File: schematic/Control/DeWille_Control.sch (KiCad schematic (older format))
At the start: 24 parts, among them J101 HN2x10, J102 HN2x10, J103 HN2x10, U101 Logo

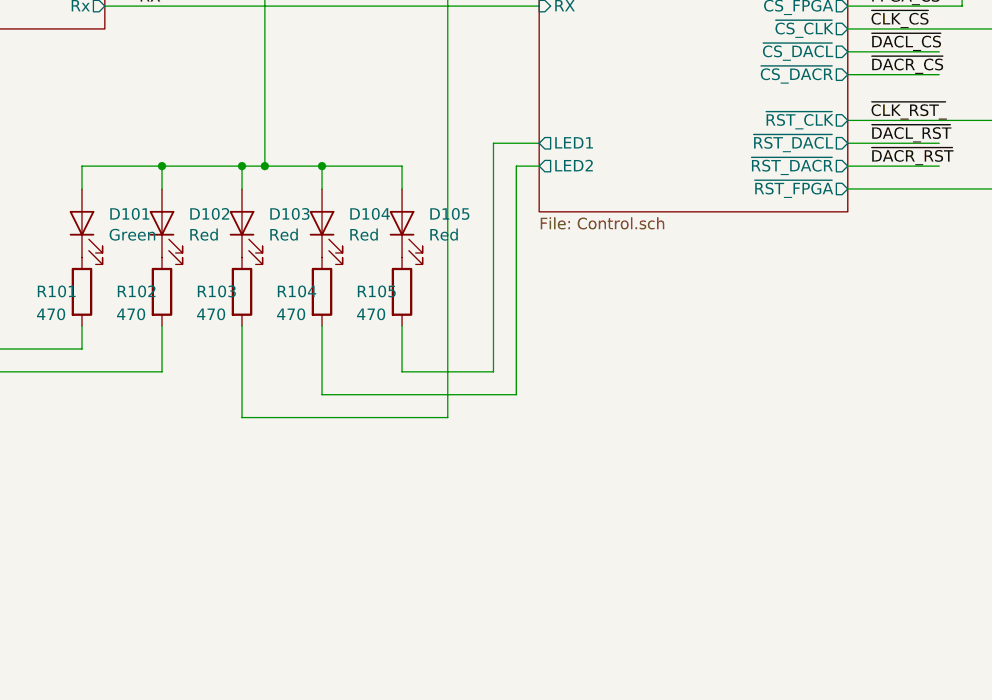
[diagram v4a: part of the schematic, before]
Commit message: Add some testpads. Fix +3V3_FPGA track mix-up after termination addition.
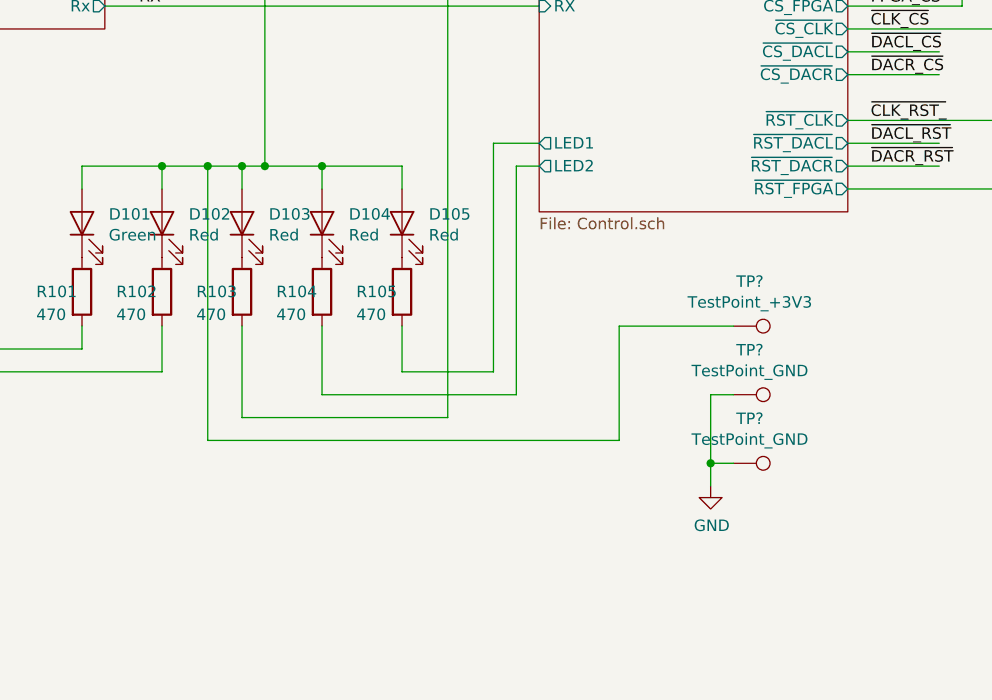
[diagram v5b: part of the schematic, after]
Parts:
- added TP? (x2): TestPoint_GND, TestPoint:TestPoint_THTPad_D2.0mm_Drill1.0mm, symbol Connector:TestPoint
- added TP?: TestPoint_+3V3, TestPoint:TestPoint_THTPad_D2.0mm_Drill1.0mm, symbol Connector:TestPoint
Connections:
- wire segments 227 -> 236
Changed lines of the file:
@@
 Connection ~ 5050 7300
 Wire Wire Line
-	4350 7300 4700 7300
+	4350 7300 4550 7300
 Wire Wire Line
 	4000 8100 2550 8100
@@
 	1    0    0    -1
 $EndComp
+$Comp
+L Connector:TestPoint TP?
+U 1 1 5DE66F70
+P 6850 8600
+AR Path="/5DCFEDFC/5DE66F70" Ref="TP?"  Part="1"
+AR Path="/5DE66F70" Ref="TP?"  Part="1"
+F 0 "TP?" V 7045 8672 50  0000 C CNN
+F 1 "TestPoint_GND" V 6954 8672 50  0000 C CNN
+F 2 "TestPoint:TestPoint_THTPad_D2.0mm_Drill1.0mm" H 7050 8600 50  0001 C CNN
+F 3 "~" H 7050 8600 50  0001 C CNN
+	1    6850 8600
+	0    1    -1   0
+$EndComp
+$Comp
+L Connector:TestPoint TP?
+U 1 1 5DE78F7B
+P 6850 8000
+AR Path="/5DCFEDFC/5DE78F7B" Ref="TP?"  Part="1"
+AR Path="/5DE78F7B" Ref="TP?"  Part="1"
+F 0 "TP?" V 7045 8072 50  0000 C CNN
+F 1 "TestPoint_+3V3" V 6954 8072 50  0000 C CNN
+F 2 "TestPoint:TestPoint_THTPad_D2.0mm_Drill1.0mm" H 7050 8000 50  0001 C CNN
+F 3 "~" H 7050 8000 50  0001 C CNN
+	1    6850 8000
+	0    1    -1   0
+$EndComp
+$Comp
+L Connector:TestPoint TP?
+U 1 1 5DE8BB1B
+P 6850 8300
+AR Path="/5DCFEDFC/5DE8BB1B" Ref="TP?"  Part="1"
+AR Path="/5DE8BB1B" Ref="TP?"  Part="1"
+F 0 "TP?" V 7045 8372 50  0000 C CNN
+F 1 "TestPoint_GND" V 6954 8372 50  0000 C CNN
+F 2 "TestPoint:TestPoint_THTPad_D2.0mm_Drill1.0mm" H 7050 8300 50  0001 C CNN
+F 3 "~" H 7050 8300 50  0001 C CNN
+	1    6850 8300
+	0    1    -1   0
+$EndComp
+$Comp
+L power:GND #PWR?
+U 1 1 5DEB2F33
+P 6750 8700
+AR Path="/5DD2C0D9/5DEB2F33" Ref="#PWR?"  Part="1"
+AR Path="/5DEB2F33" Ref="#PWR?"  Part="1"
+F 0 "#PWR?" H 6750 8450 50  0001 C CNN
+F 1 "GND" H 6755 8527 50  0000 C CNN
+F 2 "" H 6750 8700 50  0001 C CNN
+F 3 "" H 6750 8700 50  0001 C CNN
+	1    6750 8700
+	1    0    0    -1
+$EndComp
+Wire Wire Line
+	6750 8700 6750 8600
+Wire Wire Line
+	6750 8300 6850 8300
+Wire Wire Line
+	6850 8600 6750 8600
+Connection ~ 6750 8600
+Wire Wire Line
+	6750 8600 6750 8300
+Wire Wire Line
+	4550 7300 4550 8500
+Wire Wire Line
+	4550 8500 6350 8500
+Wire Wire Line
+	6350 8500 6350 8000
+Wire Wire Line
+	6350 8000 6850 8000
+Connection ~ 4550 7300
+Wire Wire Line
+	4550 7300 4700 7300
 $EndSCHEMATC

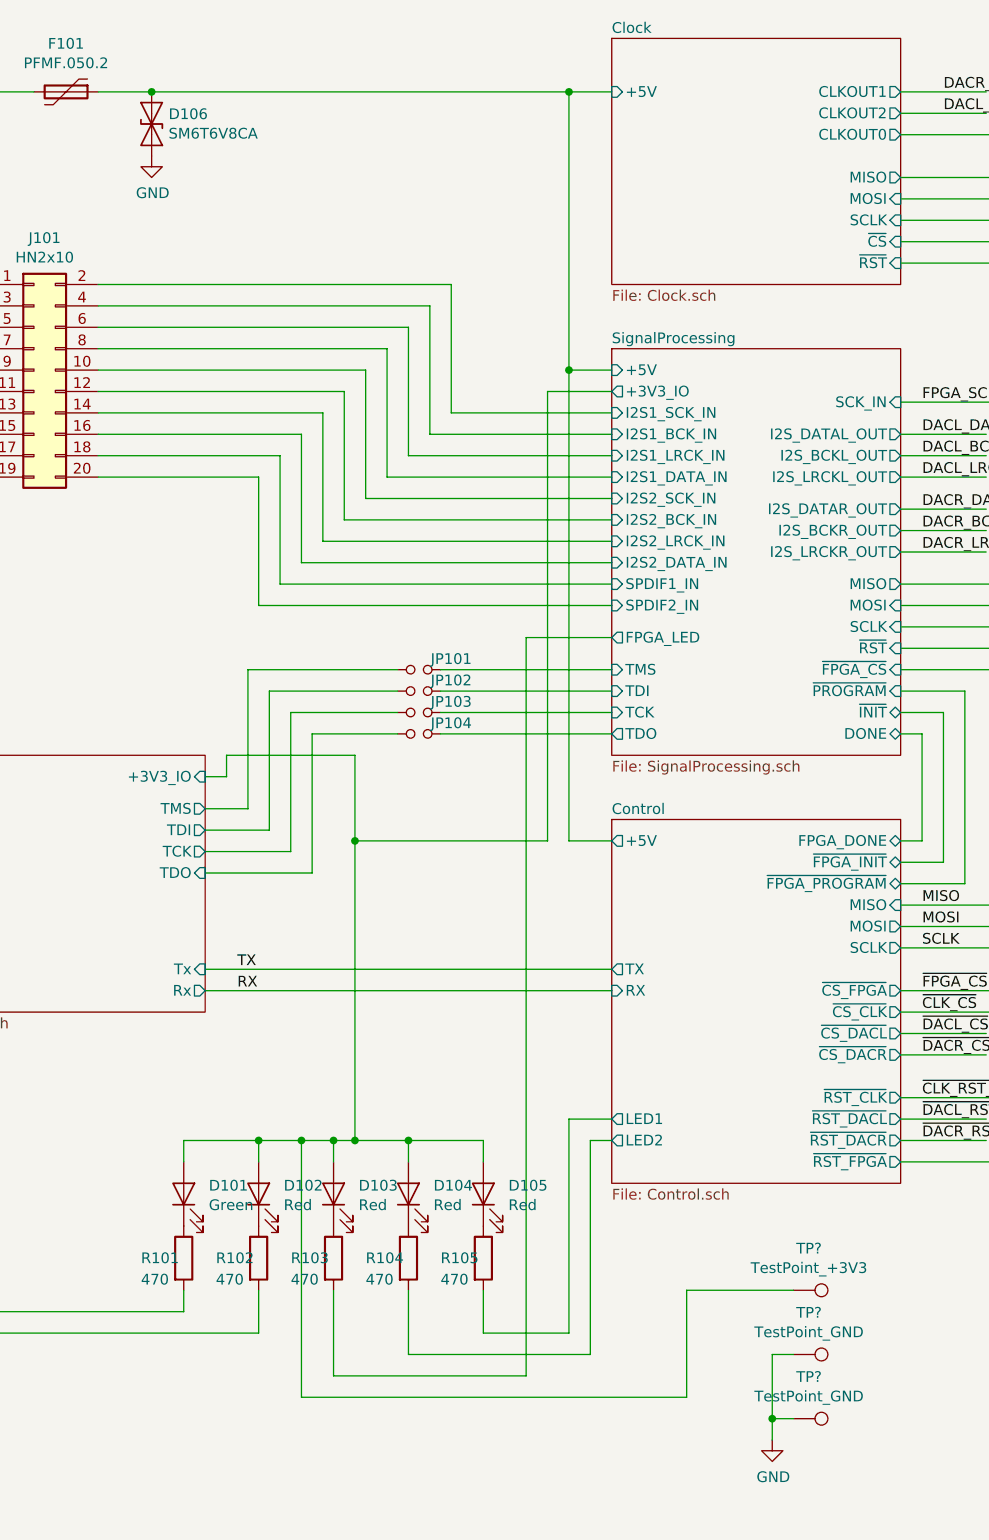
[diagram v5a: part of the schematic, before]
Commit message: Add decoupling cap between +5V and GND
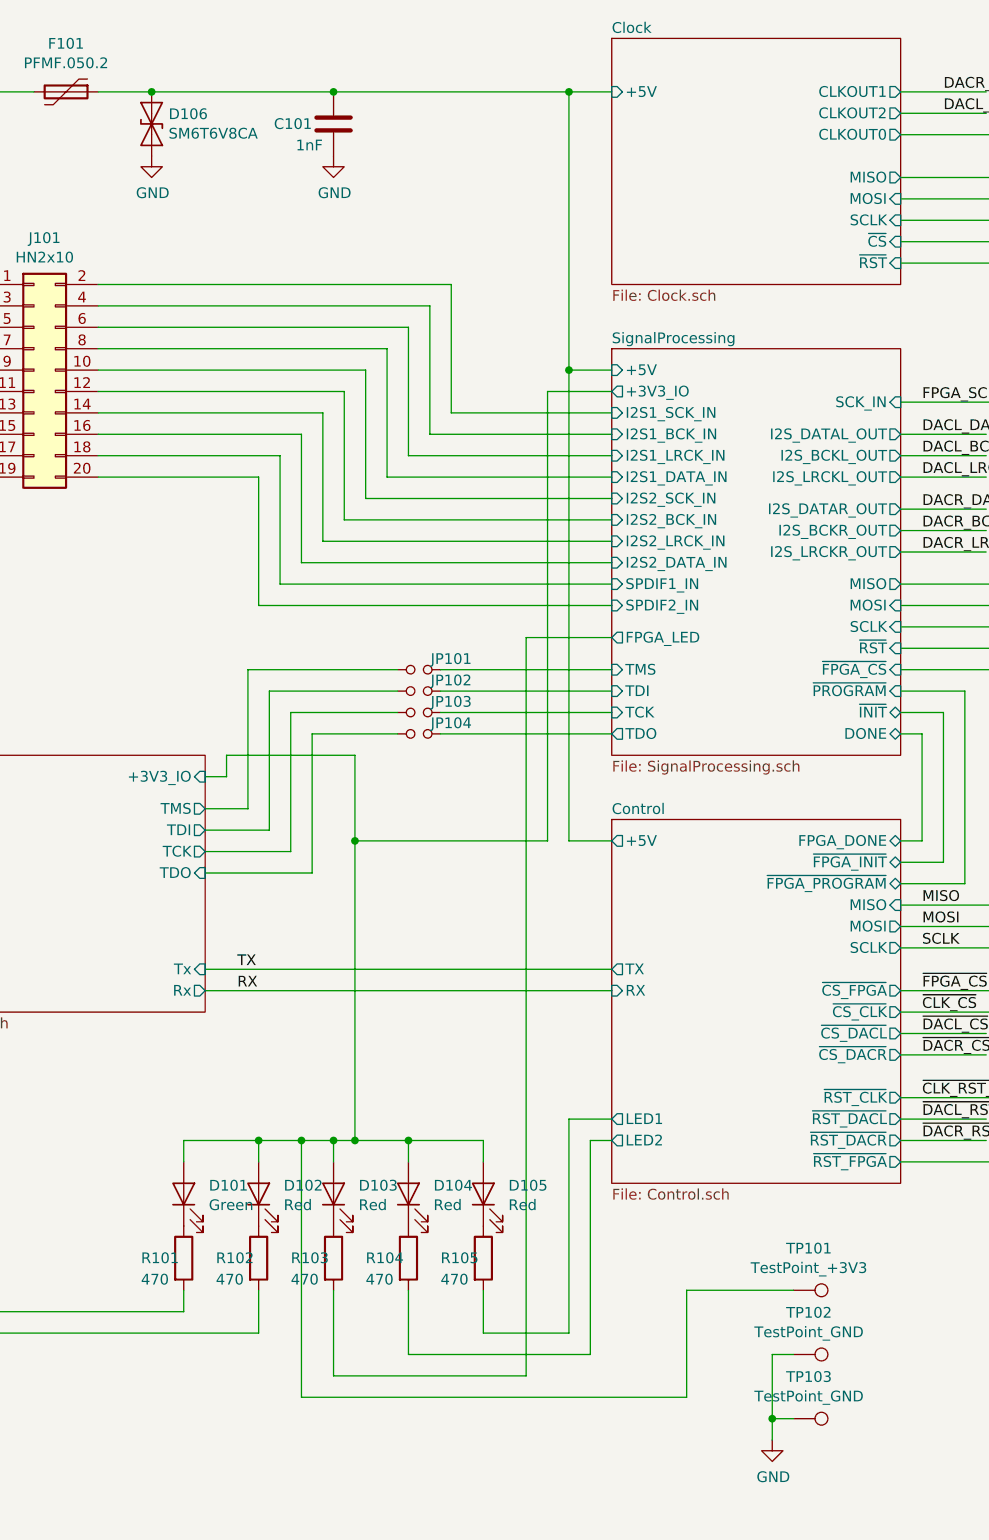
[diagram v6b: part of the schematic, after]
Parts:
- added C101: 1nF, Capacitor_SMD:C_0603_1608Metric, symbol Device:C
- gave numbers to parts that had none: 3
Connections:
- wire segments 236 -> 237
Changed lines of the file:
@@
 Connection ~ 3850 2400
 Wire Wire Line
-	3850 2400 5800 2400
+	3850 2400 4700 2400
 $Comp
 L Zmei_elements:Logo U101
@@
 P 6850 8600
 AR Path="/5DCFEDFC/5DE66F70" Ref="TP?"  Part="1"
-AR Path="/5DE66F70" Ref="TP?"  Part="1"
-F 0 "TP?" V 7045 8672 50  0000 C CNN
+AR Path="/5DE66F70" Ref="TP103"  Part="1"
+F 0 "TP103" V 7045 8672 50  0000 C CNN
 F 1 "TestPoint_GND" V 6954 8672 50  0000 C CNN
 F 2 "TestPoint:TestPoint_THTPad_D2.0mm_Drill1.0mm" H 7050 8600 50  0001 C CNN
@@
 P 6850 8000
 AR Path="/5DCFEDFC/5DE78F7B" Ref="TP?"  Part="1"
-AR Path="/5DE78F7B" Ref="TP?"  Part="1"
-F 0 "TP?" V 7045 8072 50  0000 C CNN
+AR Path="/5DE78F7B" Ref="TP101"  Part="1"
+F 0 "TP101" V 7045 8072 50  0000 C CNN
 F 1 "TestPoint_+3V3" V 6954 8072 50  0000 C CNN
 F 2 "TestPoint:TestPoint_THTPad_D2.0mm_Drill1.0mm" H 7050 8000 50  0001 C CNN
@@
 P 6850 8300
 AR Path="/5DCFEDFC/5DE8BB1B" Ref="TP?"  Part="1"
-AR Path="/5DE8BB1B" Ref="TP?"  Part="1"
-F 0 "TP?" V 7045 8372 50  0000 C CNN
+AR Path="/5DE8BB1B" Ref="TP102"  Part="1"
+F 0 "TP102" V 7045 8372 50  0000 C CNN
 F 1 "TestPoint_GND" V 6954 8372 50  0000 C CNN
 F 2 "TestPoint:TestPoint_THTPad_D2.0mm_Drill1.0mm" H 7050 8300 50  0001 C CNN
@@
 P 6750 8700
 AR Path="/5DD2C0D9/5DEB2F33" Ref="#PWR?"  Part="1"
-AR Path="/5DEB2F33" Ref="#PWR?"  Part="1"
-F 0 "#PWR?" H 6750 8450 50  0001 C CNN
+AR Path="/5DEB2F33" Ref="#PWR0150"  Part="1"
+F 0 "#PWR0150" H 6750 8450 50  0001 C CNN
 F 1 "GND" H 6755 8527 50  0000 C CNN
 F 2 "" H 6750 8700 50  0001 C CNN
@@
 Wire Wire Line
 	4550 7300 4700 7300
+$Comp
+L Device:C C?
+U 1 1 5DF13114
+P 4700 2550
+AR Path="/5DBF9B5A/5DF13114" Ref="C?"  Part="1"
+AR Path="/5DC88EF1/5DF13114" Ref="C?"  Part="1"
+AR Path="/5DCC3140/5DF13114" Ref="C?"  Part="1"
+AR Path="/5DD2C0D9/5DF13114" Ref="C?"  Part="1"
+AR Path="/5DCFEDFC/5DF13114" Ref="C?"  Part="1"
+AR Path="/5DF13114" Ref="C101"  Part="1"
+F 0 "C101" H 4800 2550 50  0000 L CNN
+F 1 "1nF" H 4750 2650 50  0000 L CNN
+F 2 "Capacitor_SMD:C_0603_1608Metric" H 4738 2400 50  0001 C CNN
+F 3 "~" H 4700 2550 50  0001 C CNN
+	1    4700 2550
+	-1   0    0    1
+$EndComp
+$Comp
+L power:GND #PWR?
+U 1 1 5DF2648F
+P 4700 2700
+AR Path="/5DD2C0D9/5DF2648F" Ref="#PWR?"  Part="1"
+AR Path="/5DF2648F" Ref="#PWR0151"  Part="1"
+F 0 "#PWR0151" H 4700 2450 50  0001 C CNN
+F 1 "GND" H 4705 2527 50  0000 C CNN
+F 2 "" H 4700 2700 50  0001 C CNN
+F 3 "" H 4700 2700 50  0001 C CNN
+	1    4700 2700
+	1    0    0    -1
+$EndComp
+Connection ~ 4700 2400
+Wire Wire Line
+	4700 2400 5800 2400
 $EndSCHEMATC

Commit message: Swap BCK and LRCK outputs. Misc small touch-ups on the board
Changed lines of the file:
@@
 Text Label 11100 4250 0    50   ~ 0
 DACR_SCK
-Text Label 11100 4450 0    50   ~ 0
+Text Label 11100 4650 0    50   ~ 0
 DACR_BCK
 Text Label 11100 4550 0    50   ~ 0
 DACR_DATA
-Text Label 11100 4650 0    50   ~ 0
+Text Label 11100 4450 0    50   ~ 0
 DACR_LRCK
 Text Label 11050 3350 0    50   ~ 0
 DACL_DATA
-Text Label 11050 3250 0    50   ~ 0
+Text Label 11050 3450 0    50   ~ 0
 DACL_BCK
 Text Label 11050 3050 0    50   ~ 0
 DACL_SCK
-Text Label 11050 3450 0    50   ~ 0
+Text Label 11050 3250 0    50   ~ 0
 DACL_LRCK
 Text Label 11100 4850 0    50   ~ 0
